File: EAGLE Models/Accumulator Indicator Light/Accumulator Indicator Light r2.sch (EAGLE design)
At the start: 9 parts, among them U1 LR8DPACK

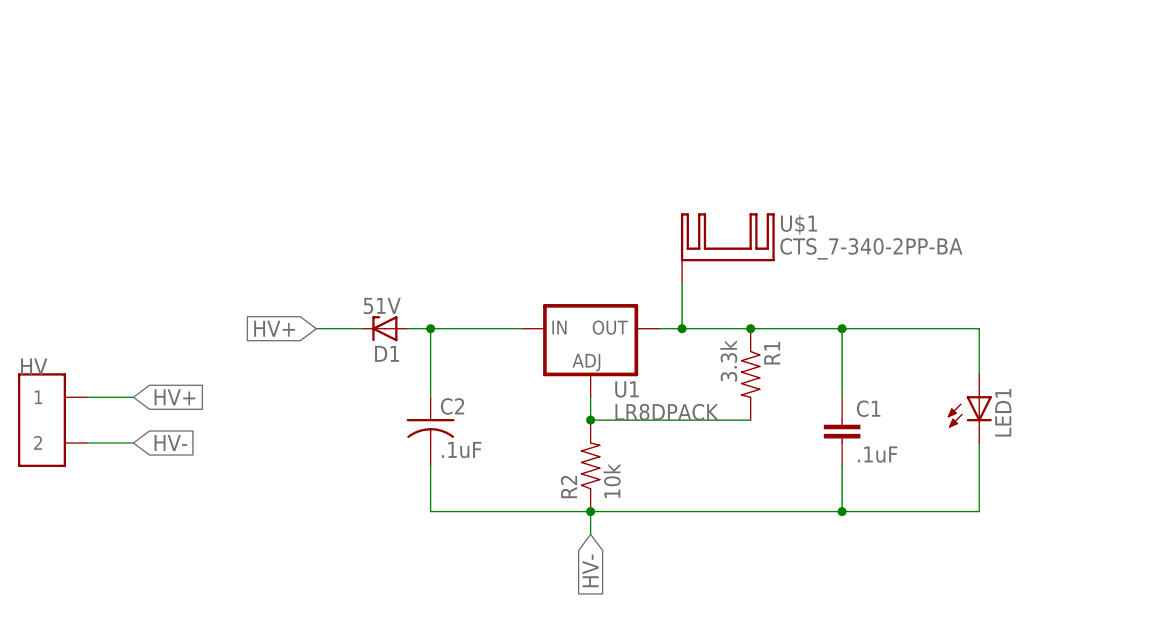
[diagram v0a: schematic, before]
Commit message: Fixed problem with AIL
Zener was too small and board was not fused
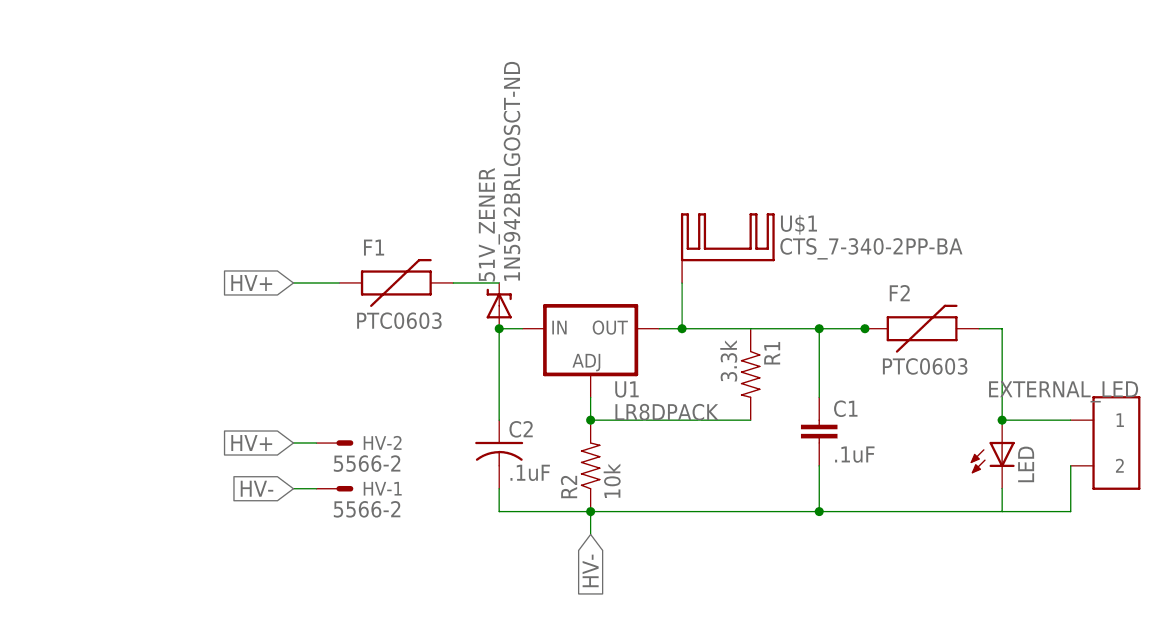
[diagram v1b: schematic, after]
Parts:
- removed D1: 51V, diode:ZENER-DIODESOT23
- removed LED1: (no value), led:LEDSMT1206
- added 51V_ZENER: 1N5942BRLGOSCT-ND, SparkFun-DiscreteSemi:DIODE-ZENERPTH
- added EXTERNAL_LED: CONN_2, formula electric:CONN_2
- added F1, F2: PTC0603, SparkFun-PowerIC:PTC0603
- added LED: (no value), led:LEDSMT1206
- HV: value CONN_2 -> 5566-2; device formula electric:CONN_2 -> con-molex:5566-2
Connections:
- new net N$10: EXTERNAL_LED.1, F2.2, LED.A
- new net N$8: 51V_ZENER.C, F1.2
- net HV+: now also F1.1, HV-2.S; no longer D1.C, HV.1
- net HV-: now also EXTERNAL_LED.2, HV-1.S, LED.C; no longer HV.2, LED1.C
- net N$: now also 51V_ZENER.A; no longer D1.A
- net N$2: now also F2.1; no longer LED1.A
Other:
- moved on the sheet: C1, C2
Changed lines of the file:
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@@
 <?xml version="1.0" encoding="utf-8"?>
 <!DOCTYPE eagle SYSTEM "eagle.dtd">
-<eagle version="7.1.0">
+<eagle version="7.2.0">
 <drawing>
 <settings>
@@
 </classes>
 <parts>
-<part name="HV" library="formula electric" deviceset="CONN_2" device=""/>
 <part name="U1" library="microchip" deviceset="LR8" device="DPACK"/>
 <part name="R1" library="SparkFun-Resistors" deviceset="RESISTOR" device="0603" value="3.3k"/>
@@
 <part name="C1" library="SparkFun-Capacitors" deviceset="CAP" device="0603-CAP" value=".1uF"/>
 <part name="C2" library="resistor" deviceset="C-US" device="C2220" value=".1uF"/>
-<part name="D1" library="diode" deviceset="ZENER-DIODE" device="SOT23" value="51V"/>
 <part name="U$1" library="heatsink" deviceset="CTS_7-340-2PP-BA" device=""/>
-<part name="LED1" library="led" deviceset="LED" device="SMT1206"/>
+<part name="LED" library="led" deviceset="LED" device="SMT1206"/>
+<part name="51V_ZENER" library="SparkFun-DiscreteSemi" deviceset="DIODE-ZENER" device="PTH" value="1N5942BRLGOSCT-ND"/>
+<part name="F1" library="SparkFun-PowerIC" deviceset="PTC" device="0603"/>
+<part name="EXTERNAL_LED" library="formula electric" deviceset="CONN_2" device=""/>
+<part name="F2" library="SparkFun-PowerIC" deviceset="PTC" device="0603"/>
+<part name="HV" library="con-molex" deviceset="5566-2" device=""/>
 </parts>
 <sheets>
@@
 </plain>
 <instances>
-<instance part="HV" gate="G$1" x="5.08" y="53.34"/>
 <instance part="U1" gate="G$1" x="66.04" y="60.96"/>
 <instance part="R1" gate="G$1" x="83.82" y="58.42" rot="R270"/>
 <instance part="R2" gate="G$1" x="66.04" y="48.26" rot="R90"/>
-<instance part="C1" gate="G$1" x="93.98" y="50.8"/>
-<instance part="C2" gate="G$1" x="48.26" y="53.34"/>
-<instance part="D1" gate="G$1" x="43.18" y="63.5" rot="R180"/>
+<instance part="C1" gate="G$1" x="91.44" y="50.8"/>
+<instance part="C2" gate="G$1" x="55.88" y="50.8"/>
 <instance part="U$1" gate="G$1" x="81.28" y="71.12"/>
-<instance part="LED1" gate="G$1" x="109.22" y="55.88"/>
+<instance part="LED" gate="G$1" x="111.76" y="50.8"/>
+<instance part="51V_ZENER" gate="G$1" x="55.88" y="66.04" rot="R90"/>
+<instance part="F1" gate="G$1" x="43.18" y="68.58"/>
+<instance part="EXTERNAL_LED" gate="G$1" x="124.46" y="50.8" rot="MR0"/>
+<instance part="F2" gate="G$1" x="101.6" y="63.5"/>
+<instance part="HV" gate="-1" x="38.1" y="45.72" rot="MR180"/>
+<instance part="HV" gate="-2" x="38.1" y="50.8" rot="MR180"/>
 </instances>
 <busses>
@@
 <net name="HV+" class="0">
 <segment>
-<pinref part="HV" gate="G$1" pin="1"/>
-<wire x1="10.16" y1="55.88" x2="15.24" y2="55.88" width="0.1524" layer="91"/>
-<label x="15.24" y="55.88" size="1.778" layer="95" xref="yes"/>
-</segment>
-<segment>
-<pinref part="D1" gate="G$1" pin="C"/>
-<wire x1="40.64" y1="63.5" x2="35.56" y2="63.5" width="0.1524" layer="91"/>
-<label x="35.56" y="63.5" size="1.778" layer="95" rot="R180" xref="yes"/>
+<label x="33.02" y="50.8" size="1.778" layer="95" rot="R180" xref="yes"/>
+<pinref part="HV" gate="-2" pin="S"/>
+<wire x1="33.02" y1="50.8" x2="35.56" y2="50.8" width="0.1524" layer="91"/>
+</segment>
+<segment>
+<label x="33.02" y="68.58" size="1.778" layer="95" rot="R180" xref="yes"/>
+<pinref part="F1" gate="G$1" pin="1"/>
+<wire x1="33.02" y1="68.58" x2="38.1" y2="68.58" width="0.1524" layer="91"/>
 </segment>
 </net>
 <net name="HV-" class="0">
 <segment>
-<pinref part="HV" gate="G$1" pin="2"/>
-<wire x1="10.16" y1="50.8" x2="15.24" y2="50.8" width="0.1524" layer="91"/>
-<label x="15.24" y="50.8" size="1.778" layer="95" xref="yes"/>
+<label x="33.02" y="45.72" size="1.778" layer="95" rot="R180" xref="yes"/>
+<pinref part="HV" gate="-1" pin="S"/>
+<wire x1="33.02" y1="45.72" x2="35.56" y2="45.72" width="0.1524" layer="91"/>
 </segment>
 <segment>
@@
 <label x="66.04" y="40.64" size="1.778" layer="95" rot="R270" xref="yes"/>
 <pinref part="C1" gate="G$1" pin="2"/>
-<wire x1="93.98" y1="48.26" x2="93.98" y2="43.18" width="0.1524" layer="91"/>
-<wire x1="93.98" y1="43.18" x2="66.04" y2="43.18" width="0.1524" layer="91"/>
+<wire x1="91.44" y1="48.26" x2="91.44" y2="43.18" width="0.1524" layer="91"/>
+<wire x1="91.44" y1="43.18" x2="66.04" y2="43.18" width="0.1524" layer="91"/>
 <junction x="66.04" y="43.18"/>
-<wire x1="109.22" y1="50.8" x2="109.22" y2="43.18" width="0.1524" layer="91"/>
-<wire x1="109.22" y1="43.18" x2="93.98" y2="43.18" width="0.1524" layer="91"/>
-<junction x="93.98" y="43.18"/>
+<wire x1="111.76" y1="45.72" x2="111.76" y2="43.18" width="0.1524" layer="91"/>
+<wire x1="111.76" y1="43.18" x2="91.44" y2="43.18" width="0.1524" layer="91"/>
+<junction x="91.44" y="43.18"/>
 <pinref part="C2" gate="G$1" pin="2"/>
-<wire x1="48.26" y1="48.26" x2="48.26" y2="43.18" width="0.1524" layer="91"/>
-<wire x1="48.26" y1="43.18" x2="66.04" y2="43.18" width="0.1524" layer="91"/>
-<pinref part="LED1" gate="G$1" pin="C"/>
+<wire x1="55.88" y1="45.72" x2="55.88" y2="43.18" width="0.1524" layer="91"/>
+<wire x1="55.88" y1="43.18" x2="66.04" y2="43.18" width="0.1524" layer="91"/>
+<pinref part="LED" gate="G$1" pin="C"/>
+<pinref part="EXTERNAL_LED" gate="G$1" pin="2"/>
+<wire x1="119.38" y1="48.26" x2="119.38" y2="43.18" width="0.1524" layer="91"/>
+<wire x1="119.38" y1="43.18" x2="111.76" y2="43.18" width="0.1524" layer="91"/>
 </segment>
 </net>
@@
 <pinref part="R1" gate="G$1" pin="1"/>
 <wire x1="83.82" y1="63.5" x2="76.2" y2="63.5" width="0.1524" layer="91"/>
-<pinref part="C1" gate="G$1" pin="1"/>
 <wire x1="76.2" y1="63.5" x2="73.66" y2="63.5" width="0.1524" layer="91"/>
-<wire x1="109.22" y1="63.5" x2="109.22" y2="58.42" width="0.1524" layer="91"/>
-<wire x1="93.98" y1="63.5" x2="109.22" y2="63.5" width="0.1524" layer="91"/>
-<wire x1="93.98" y1="63.5" x2="93.98" y2="55.88" width="0.1524" layer="91"/>
-<wire x1="83.82" y1="63.5" x2="93.98" y2="63.5" width="0.1524" layer="91"/>
-<junction x="83.82" y="63.5"/>
-<junction x="93.98" y="63.5"/>
 <pinref part="U$1" gate="G$1" pin="K@1"/>
 <wire x1="76.2" y1="68.58" x2="76.2" y2="63.5" width="0.1524" layer="91"/>
 <junction x="76.2" y="63.5"/>
-<pinref part="LED1" gate="G$1" pin="A"/>
+<pinref part="F2" gate="G$1" pin="1"/>
+<junction x="96.52" y="63.5"/>
+<wire x1="96.52" y1="63.5" x2="91.44" y2="63.5" width="0.1524" layer="91"/>
+<pinref part="C1" gate="G$1" pin="1"/>
+<wire x1="91.44" y1="63.5" x2="83.82" y2="63.5" width="0.1524" layer="91"/>
+<wire x1="91.44" y1="55.88" x2="91.44" y2="63.5" width="0.1524" layer="91"/>
+<junction x="91.44" y="63.5"/>
 </segment>
 </net>
@@
 <segment>
 <pinref part="U1" gate="G$1" pin="IN"/>
-<wire x1="58.42" y1="63.5" x2="48.26" y2="63.5" width="0.1524" layer="91"/>
+<wire x1="58.42" y1="63.5" x2="55.88" y2="63.5" width="0.1524" layer="91"/>
 <pinref part="C2" gate="G$1" pin="1"/>
-<wire x1="48.26" y1="55.88" x2="48.26" y2="63.5" width="0.1524" layer="91"/>
-<pinref part="D1" gate="G$1" pin="A"/>
-<wire x1="45.72" y1="63.5" x2="48.26" y2="63.5" width="0.1524" layer="91"/>
-<junction x="48.26" y="63.5"/>
-</segment>
-</net>
+<wire x1="55.88" y1="53.34" x2="55.88" y2="63.5" width="0.1524" layer="91"/>
+<junction x="55.88" y="63.5"/>
+<pinref part="51V_ZENER" gate="G$1" pin="A"/>
+</segment>
+</net>
+<net name="N$8" class="0">
+<segment>
+<pinref part="F1" gate="G$1" pin="2"/>
+<pinref part="51V_ZENER" gate="G$1" pin="C"/>
+<wire x1="50.8" y1="68.58" x2="55.88" y2="68.58" width="0.1524" layer="91"/>
+</segment>
+</net>
+<net name="N$10" class="0">
+<segment>
+<pinref part="EXTERNAL_LED" gate="G$1" pin="1"/>
+<pinref part="LED" gate="G$1" pin="A"/>
+<wire x1="119.38" y1="53.34" x2="111.76" y2="53.34" width="0.1524" layer="91"/>
+<wire x1="111.76" y1="53.34" x2="111.76" y2="63.5" width="0.1524" layer="91"/>
+<wire x1="109.22" y1="63.5" x2="111.76" y2="63.5" width="0.1524" layer="91"/>
+<junction x="111.76" y="53.34"/>
+<pinref part="F2" gate="G$1" pin="2"/>
+</segment>
+</net>
